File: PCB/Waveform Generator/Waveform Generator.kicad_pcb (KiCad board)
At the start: 4 copper layers, 124 parts, among them J1 Power input, J10 I2C1, J11 5001, J12 5001, J13 5001, J14 5001, J15 5001, J16 5001, J17 5001, J18 5001, J2 RS485, J3 USB_B_Micro, J4 Signal 1, J5 Signal 2, J6 SWD, J7 USART1, J8 TIMER, J9 ADC, Q0 AO3401A, Q1 Q_NPN_BCE, Q2 Q_NPN_BCE, Q3 Q_PNP_BCE, Q4 Q_NPN_BCE, Q5 Q_NPN_BCE, Q6 Q_NPN_BCE, SW1 SW_SPDT, SW2 RESET Button, SW3 SW_SPDT, SW4 Btn1, SW5 Btn1, SW6 Btn1, U1 STM32F405RGT6, U2 MAX485E, U3 USBLC6-2SC6, U4 OPAMP, U5 OPAMP, U6 OPAMP, U7 OPAMP, U8 LM335ADT

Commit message: Starting PCB layout
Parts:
- removed U6, U7: OPAMP, Package_SO:MSOP-8-1EP_3x3mm_P0.65mm_EP1.68x1.88mm
- J12: value 5001 -> Signal 2; footprint Extra Components:5001 Test Point -> TerminalBlock_MetzConnect:TerminalBlock_MetzConnect_Type086_RT03402HBLC_1x02_P3.81mm_Horizontal
- J4: value Signal 1 -> 5001; footprint TerminalBlock_MetzConnect:TerminalBlock_MetzConnect_Type086_RT03402HBLC_1x02_P3.81mm_Horizontal -> Extra Components:5001 Test Point
- U4, U5: value OPAMP -> LTC2051HVIMS8; footprint Package_SO:MSOP-8-1EP_3x3mm_P0.65mm_EP1.68x1.88mm -> Package_SO:MSOP-8-1EP_3x3mm_P0.65mm_EP1.73x1.85mm
- moved R13 307.6 mm to (479.3, -138.4)
- moved C13 289.1 mm to (511.3, -121.9)
- moved C12 273.3 mm to (511.8, -105.4)
- moved C11 272.4 mm to (504.2, -127.0)
- moved R12 233.5 mm to (416.6, -94.0)
- moved J15 210.3 mm to (195.4, -100.2)
- moved R23 209.4 mm to (332.4, -122.6)
- moved R27 209.4 mm to (338.2, -122.6)
- moved R25 209.4 mm to (335.3, -122.6)
- moved C25 200.5 mm to (408.5, -85.1)
- moved Q4 199.0 mm to (307.3, -161.3)
- moved R30 198.3 mm to (365.7, 112.4)
- moved R32 198.3 mm to (371.5, 112.4)
- moved R31 198.3 mm to (368.6, 112.4)
- moved R29 197.9 mm to (365.3, 106.7)
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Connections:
- J11 pad 1: (no net) -> Net-(J11-Pad1)
- J12 pad 1: (no net) -> Net-(J11-Pad1)
- J5 pad 1: Net-(J5-Pad1) -> Net-(J4-Pad1)
- R22 pad 1: Net-(J5-Pad1) -> Net-(J11-Pad1)
- U4 pad 1: GND -> Net-(R16-Pad1)
- U4 pad 3: Net-(R16-Pad1) -> GND
- U4 pad 4: +5V -> -5V
- U4 pad 5: -5V -> GND
- U4 pad 6: (no net) -> Net-(C28-Pad2)
- U4 pad 7: (no net) -> Net-(J4-Pad1)
- U4 pad 8: (no net) -> +5V
- U5 pad 1: GND -> Net-(R20-Pad1)
- U5 pad 2: Net-(C28-Pad2) -> Net-(C29-Pad2)
- U5 pad 3: Net-(J4-Pad1) -> GND
- U5 pad 4: +5V -> -5V
- U5 pad 5: -5V -> GND
- U5 pad 6: (no net) -> Net-(C30-Pad2)
- U5 pad 7: (no net) -> Net-(J11-Pad1)
- U5 pad 8: (no net) -> +5V

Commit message: update!
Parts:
- moved J18 497.3 mm to (105.5, 74.3)
- moved H2 466.8 mm to (107.0, 139.2)
- moved H3 460.5 mm to (107.6, 62.2)
- moved SW3 448.7 mm to (106.8, 98.9), turned to 270 degrees
- moved SW6 439.4 mm to (178.3, 141.0), turned to 90 degrees
- moved R13 437.3 mm to (112.5, 99.7)
- moved C11 425.0 mm to (168.9, 134.2), turned to 180 degrees
- moved SW5 421.7 mm to (187.4, 140.3), turned to 90 degrees
- moved C13 419.8 mm to (178.5, 134.0), turned to 180 degrees
- moved SW2 417.4 mm to (149.4, 115.5)
- moved SW4 410.0 mm to (168.8, 140.9), turned to 90 degrees
- moved C12 403.2 mm to (187.0, 133.5), turned to 180 degrees
- moved H4 377.5 mm to (218.9, 142.1)
- moved U8 376.8 mm to (148.8, 94.9)
- moved J17 376.7 mm to (156.8, 93.2)
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
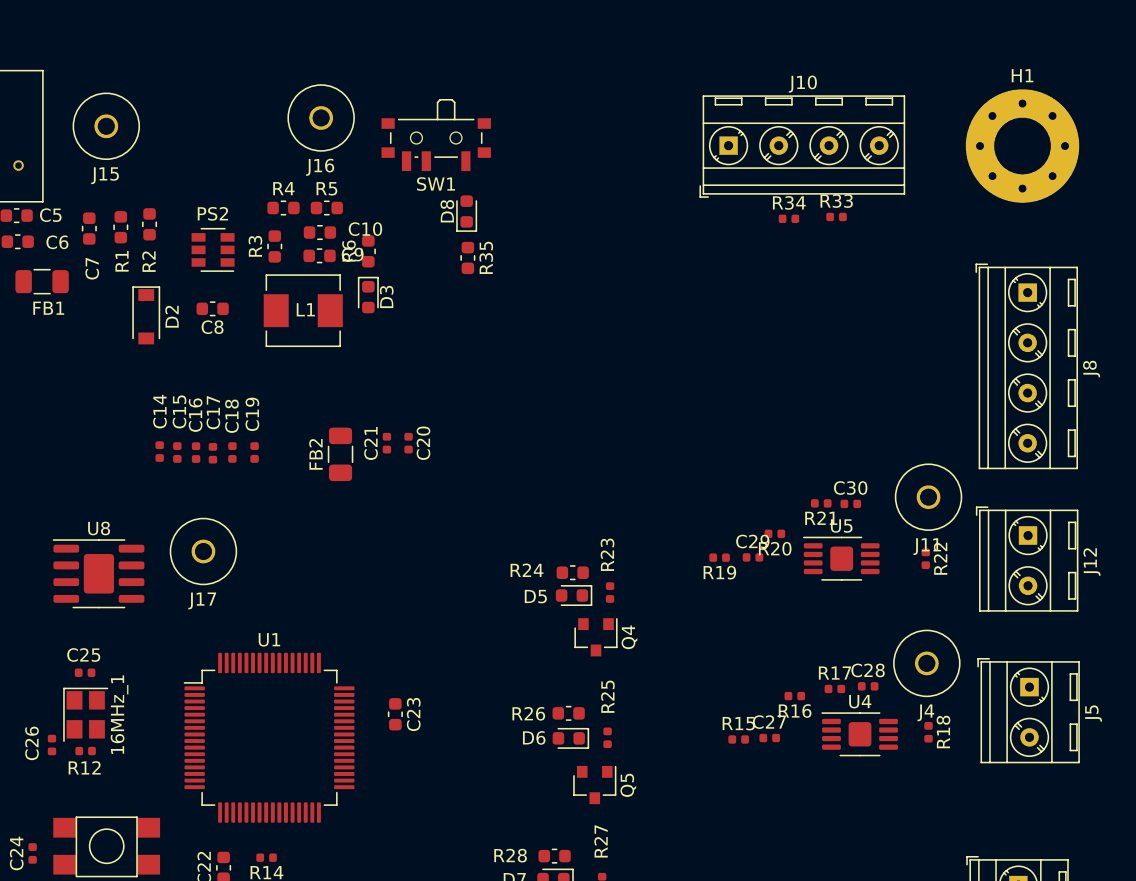
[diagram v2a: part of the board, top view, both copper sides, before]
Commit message: Updating op-amps and powersupply
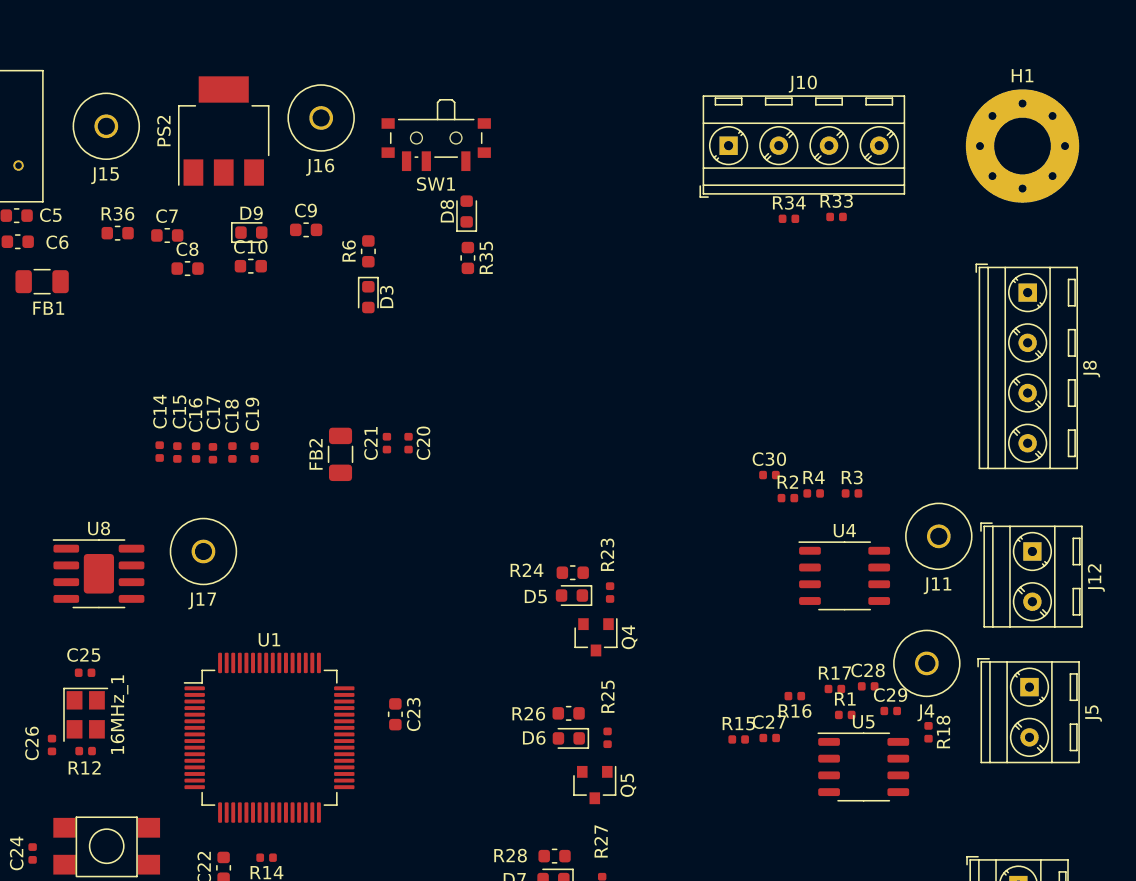
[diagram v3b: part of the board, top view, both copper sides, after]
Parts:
- removed D2: B5819W, Diode_SMD:D_SOD-123
- removed L1: 10u, Inductor_SMD:L_Sunlord_MWSA0518_5.4x5.2mm
- removed R19, R20, R21, R22: 1k, Resistor_SMD:R_0402_1005Metric
- removed R5: 270, Resistor_SMD:R_0603_1608Metric
- added D9: GREEN, LED_SMD:LED_0603_1608Metric, F.Cu at (160.4, 69.0)
- added R36: 1k, Resistor_SMD:R_0603_1608Metric, F.Cu at (150.2, 69.0)
- C8: value 10n -> 0.1u
- C9: value 10u -> 0.1u
- PS1: value ITP0312D05 -> ITP0324D05
- PS2: value MP2359DJ-LF-Z -> AMS1117-3.3; footprint Package_TO_SOT_SMD:SOT-23-6 -> Package_TO_SOT_SMD:SOT-223-3_TabPin2
- R1: value 100k -> 1k; footprint Resistor_SMD:R_0603_1608Metric -> Resistor_SMD:R_0402_1005Metric
- R2: value 68k -> 1k; footprint Resistor_SMD:R_0603_1608Metric -> Resistor_SMD:R_0402_1005Metric
- R3: value 47k -> 1k; footprint Resistor_SMD:R_0603_1608Metric -> Resistor_SMD:R_0402_1005Metric
- R4: value 15k -> 1k; footprint Resistor_SMD:R_0603_1608Metric -> Resistor_SMD:R_0402_1005Metric
- U4, U5: value LTC2051HVIMS8 -> OPA1602; footprint Package_SO:MSOP-8-1EP_3x3mm_P0.65mm_EP1.73x1.85mm -> Package_SO:SOP-8_3.9x4.9mm_P1.27mm
- moved R1 66.3 mm to (205.4, 105.6), turned to 0 degrees
- moved R2 52.7 mm to (201.1, 89.2), turned to 0 degrees
- moved R3 47.6 mm to (206.0, 88.8), turned to 0 degrees
- moved R4 45.7 mm to (203.1, 88.8)
- moved U5 15.9 mm to (206.8, 109.5)
- moved C29 15.7 mm to (208.9, 105.3)
- moved U4 12.1 mm to (205.4, 95.0)
- moved PS2 9.06 mm to (158.3, 61.3), turned to 90 degrees
- moved C30 6.55 mm to (199.7, 87.4)
- moved C7 5.94 mm to (154.0, 69.2), turned to 0 degrees
- moved C10 5.83 mm to (160.4, 71.6)
- moved C8 3.60 mm to (155.6, 71.7), turned to 0 degrees
- moved J11 3.07 mm to (212.6, 92.0)
- moved C9 2.22 mm to (164.6, 68.8)
- moved J12 1.25 mm to (219.7, 93.2)
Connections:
- C10 pad 1: GND -> Net-(C10-Pad1)
- C10 pad 2: Net-(C10-Pad2) -> GND
- C7 pad 1: GND -> +5V
- C7 pad 2: +5V -> GND
- C8 pad 1: Net-(C8-Pad1) -> +5V
- C8 pad 2: Net-(C8-Pad2) -> GND
- C9 pad 1: GND -> Net-(C10-Pad1)
- C9 pad 2: Net-(C10-Pad2) -> GND
- D3 pad 2: Net-(C10-Pad2) -> Net-(C10-Pad1)
- J16 pad 1: Net-(C10-Pad2) -> Net-(C10-Pad1)
- PS2 pad 1: Net-(C8-Pad1) -> (no net)
- PS2 pad 2: GND -> Net-(C10-Pad1)
- PS2 pad 3: Net-(PS2-Pad3) -> +5V
- R1 pad 1: +5V -> Net-(C29-Pad1)
- R1 pad 2: Net-(PS2-Pad4) -> Net-(R1-Pad2)
- R16 pad 1: Net-(R16-Pad1) -> Net-(C27-Pad2)
- R16 pad 2: Net-(C27-Pad2) -> Net-(R16-Pad2)
- R17 pad 2: Net-(R16-Pad1) -> Net-(R16-Pad2)
- R2 pad 1: Net-(PS2-Pad4) -> Net-(C30-Pad1)
- R2 pad 2: GND -> DAC_OUT2
- R3 pad 1: Net-(C10-Pad2) -> Net-(J11-Pad1)
- R3 pad 2: Net-(PS2-Pad3) -> Net-(C29-Pad2)
- R4 pad 1: Net-(PS2-Pad3) -> Net-(C30-Pad2)
- R4 pad 2: Net-(R4-Pad2) -> Net-(R1-Pad2)
- SW1 pad 2: Net-(C10-Pad2) -> Net-(C10-Pad1)
- U4 pad 1: Net-(R16-Pad1) -> Net-(R16-Pad2)
- U5 pad 1: Net-(R20-Pad1) -> Net-(R1-Pad2)
- U5 pad 2: Net-(C29-Pad2) -> Net-(C30-Pad2)
- U5 pad 6: Net-(C30-Pad2) -> Net-(C29-Pad2)

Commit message: Making updates to schematic
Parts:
- moved C29 15.0 mm to (208.2, 90.3)
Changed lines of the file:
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@@
   )
   (module Capacitor_SMD:C_0402_1005Metric (layer F.Cu)
-    (at 208.9 105.3)
+    (at 208.165 90.3)
     (descr "Capacitor SMD 0402 (1005 Metric), square (rectangular) end terminal, IPC_7351 nominal, (Body size source: http://www.tortai-tech.com/upload/download/2011102023233369053.pdf), generated with kicad-footprint-generator")
     (tags capacitor)
@@
       (effects (font (size 1 1) (thickness 0.15)))
     )
+    (fp_line (start -0.5 0.25) (end -0.5 -0.25) (layer F.Fab) (width 0.1))
+    (fp_line (start -0.5 -0.25) (end 0.5 -0.25) (layer F.Fab) (width 0.1))
+    (fp_line (start 0.5 -0.25) (end 0.5 0.25) (layer F.Fab) (width 0.1))
+    (fp_line (start 0.5 0.25) (end -0.5 0.25) (layer F.Fab) (width 0.1))
+    (fp_line (start -0.93 0.47) (end -0.93 -0.47) (layer F.CrtYd) (width 0.05))
+    (fp_line (start -0.93 -0.47) (end 0.93 -0.47) (layer F.CrtYd) (width 0.05))
+    (fp_line (start 0.93 -0.47) (end 0.93 0.47) (layer F.CrtYd) (width 0.05))
+    (fp_line (start 0.93 0.47) (end -0.93 0.47) (layer F.CrtYd) (width 0.05))
     (fp_text user %R (at 0 0) (layer F.Fab)
       (effects (font (size 0.25 0.25) (thickness 0.04)))
     )
-    (fp_line (start 0.93 0.47) (end -0.93 0.47) (layer F.CrtYd) (width 0.05))
-    (fp_line (start 0.93 -0.47) (end 0.93 0.47) (layer F.CrtYd) (width 0.05))
-    (fp_line (start -0.93 -0.47) (end 0.93 -0.47) (layer F.CrtYd) (width 0.05))
-    (fp_line (start -0.93 0.47) (end -0.93 -0.47) (layer F.CrtYd) (width 0.05))
-    (fp_line (start 0.5 0.25) (end -0.5 0.25) (layer F.Fab) (width 0.1))
-    (fp_line (start 0.5 -0.25) (end 0.5 0.25) (layer F.Fab) (width 0.1))
-    (fp_line (start -0.5 -0.25) (end 0.5 -0.25) (layer F.Fab) (width 0.1))
-    (fp_line (start -0.5 0.25) (end -0.5 -0.25) (layer F.Fab) (width 0.1))
+    (pad 1 smd roundrect (at -0.485 0) (size 0.59 0.64) (layers F.Cu F.Paste F.Mask) (roundrect_rratio 0.25)
+      (net 20 "Net-(C29-Pad1)"))
     (pad 2 smd roundrect (at 0.485 0) (size 0.59 0.64) (layers F.Cu F.Paste F.Mask) (roundrect_rratio 0.25)
       (net 86 "Net-(R1-Pad2)"))
-    (pad 1 smd roundrect (at -0.485 0) (size 0.59 0.64) (layers F.Cu F.Paste F.Mask) (roundrect_rratio 0.25)
-      (net 20 "Net-(C29-Pad1)"))
     (model ${KISYS3DMOD}/Resistor_SMD.3dshapes/R_0402_1005Metric.wrl
       (at (xyz 0 0 0))

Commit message: Making progress with PCB layout
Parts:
- added D10: RED, LED_SMD:LED_0603_1608Metric, F.Cu at (306.9, 133.3)
- added D2: GREEN, LED_SMD:LED_0603_1608Metric, F.Cu at (311.0, 133.3)
- added J19: ADC_2, Extra Components:5mm Pitch, 2 Way Terminal Block, F.Cu at (331.9, 98.2)
- added J20: TIMER_1, Extra Components:5mm Pitch, 2 Way Terminal Block, F.Cu at (313.4, 116.7)
- added J21: I2C1_1, Extra Components:5mm Pitch, 2 Way Terminal Block, F.Cu at (325.6, 114.3)
- added J22: TIMER_2, Extra Components:5mm Pitch, 2 Way Terminal Block, F.Cu at (344.0, 98.2)
- added J23: I2C1_2, Extra Components:5mm Pitch, 2 Way Terminal Block, F.Cu at (356.2, 98.2)
- added Q7: Q_NPN_BCE, Package_TO_SOT_SMD:SOT-23, F.Cu at (331.2, 127.2)
- added Q8: Q_NPN_BCE, Package_TO_SOT_SMD:SOT-23, F.Cu at (321.7, 131.9)
- added R19: 10k, Resistor_SMD:R_0402_1005Metric, F.Cu at (329.4, 130.6)
- added R20: 10k, Resistor_SMD:R_0402_1005Metric, F.Cu at (325.4, 133.1)
- added R21: 470, Resistor_SMD:R_0603_1608Metric, F.Cu at (325.9, 130.8)
- added R22: 470, Resistor_SMD:R_0603_1608Metric, F.Cu at (364.0, 94.0)
- added R37: 33, Resistor_SMD:R_0402_1005Metric, F.Cu at (338.9, 125.9)
- added R38: 33, Resistor_SMD:R_0402_1005Metric, F.Cu at (328.3, 133.1)
- added R39: 120, Resistor_SMD:R_0603_1608Metric, F.Cu at (335.4, 126.2)
- added R5: 10k, Resistor_SMD:R_0402_1005Metric, F.Cu at (111.5, 84.2)
- added SW7: SW_SPDT, Button_Switch_SMD:SW_SPDT_PCM12, F.Cu at (108.3, 84.1)
- added U10: USBLC6-2SC6, Package_TO_SOT_SMD:SOT-23-6, F.Cu at (317.0, 131.9)
- added U11: USBLC6-2SC6, Package_TO_SOT_SMD:SOT-23-6, F.Cu at (307.3, 129.6)
- added U6: USBLC6-2SC6, Package_TO_SOT_SMD:SOT-23-6, F.Cu at (321.7, 127.3)
- added U7: USBLC6-2SC6, Package_TO_SOT_SMD:SOT-23-6, F.Cu at (312.2, 129.6)
- added U9: USBLC6-2SC6, Package_TO_SOT_SMD:SOT-23-6, F.Cu at (326.6, 127.3)
- C22, C23: footprint Capacitor_SMD:C_0603_1608Metric -> Capacitor_SMD:C_0402_1005Metric
- C25, C26: value 12p -> 20p
- F1: value 250mA -> 300mA
- FB2: value 600 @ 600 MHz -> 600 @ 600MHz
- J10: value I2C1 -> USART1_2; footprint TerminalBlock_MetzConnect:TerminalBlock_MetzConnect_Type086_RT03404HBLC_1x04_P3.81mm_Horizontal -> Extra Components:5mm Pitch, 2 Way Terminal Block
- J2: value RS485 -> RS485_1; footprint TerminalBlock_MetzConnect:TerminalBlock_MetzConnect_Type086_RT03404HBLC_1x04_P3.81mm_Horizontal -> Extra Components:5mm Pitch, 2 Way Terminal Block
- J5: footprint TerminalBlock_MetzConnect:TerminalBlock_MetzConnect_Type086_RT03402HBLC_1x02_P3.81mm_Horizontal -> Extra Components:5mm Pitch, 2 Way Terminal Block
- J7: value USART1 -> RS485_2; footprint TerminalBlock_MetzConnect:TerminalBlock_MetzConnect_Type086_RT03404HBLC_1x04_P3.81mm_Horizontal -> Extra Components:5mm Pitch, 2 Way Terminal Block
- J8: value TIMER -> USART1_1; footprint TerminalBlock_MetzConnect:TerminalBlock_MetzConnect_Type086_RT03404HBLC_1x04_P3.81mm_Horizontal -> Extra Components:5mm Pitch, 2 Way Terminal Block
- J9: value ADC -> ADC_1; footprint TerminalBlock_MetzConnect:TerminalBlock_MetzConnect_Type086_RT03404HBLC_1x04_P3.81mm_Horizontal -> Extra Components:5mm Pitch, 2 Way Terminal Block
- U1: value STM32F405RGT6 -> STM32F427VITx; footprint Package_QFP:LQFP-64_10x10mm_P0.5mm -> Package_QFP:LQFP-100_14x14mm_P0.5mm
- U2: value MAX485E -> MAX485EESAT
- X1: renamed from 16MHz_1; value Y200 -> 25MHZ
- moved J2 217.5 mm to (361.9, 114.3), turned to 0 degrees
- moved C22 210.5 mm to (367.5, 93.7), turned to 0 degrees
- moved R14 202.9 mm to (363.5, 96.2), turned to 0 degrees
- moved C23 146.5 mm to (316.1, 128.3), turned to 0 degrees
- moved J7 142.0 mm to (349.8, 114.3), turned to 0 degrees
- moved J10 128.3 mm to (319.8, 98.2)
- moved J8 125.2 mm to (337.7, 114.3), turned to 0 degrees
- moved U1 121.2 mm to (281.4, 87.7)
- moved J9 82.7 mm to (301.3, 116.7), turned to 0 degrees
- moved J18 33.7 mm to (124.0, 46.2)
- moved D9 30.0 mm to (130.5, 71.2), turned to 90 degrees
- moved U3 23.8 mm to (113.7, 73.0), turned to 180 degrees
- moved J3 23.4 mm to (108.3, 73.1)
- moved R36 21.7 mm to (128.7, 71.2), turned to 90 degrees
- moved D3 19.1 mm to (152.4, 65.0), turned to 180 degrees
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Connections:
- C13 pad 2: BT3N_Input -> BTN3_Input
- J10 pad 1: +3V3 -> Net-(J10-Pad1)
- J10 pad 2: I2C1_SDA -> GND
- J12 pad 1: Net-(J11-Pad1) -> Net-(J12-Pad1)
- J3 pad 2: USB_CONN_D- -> Net-(J3-Pad2)
- J3 pad 3: USB_CONN_D+ -> Net-(J3-Pad3)
- J5 pad 1: Net-(J4-Pad1) -> Net-(J5-Pad1)
- J6 pad 3: GND -> Net-(J6-Pad3)
- J6 pad 5: GND -> Net-(J6-Pad5)
- J6 pad 9: GND -> Net-(J6-Pad9)
- J7 pad 1: +3V3 -> Net-(J14-Pad1)
- J7 pad 2: USART1_TX -> GND
- J8 pad 2: TIM1_CH1 -> Net-(J8-Pad2)
- J9 pad 2: ADC2_IN0 -> Net-(J9-Pad2)
- R14 pad 1: BOOT1 -> Net-(J6-Pad3)
- R33 pad 1: I2C1_SCL -> Net-(J23-Pad1)
- R34 pad 1: I2C1_SDA -> Net-(J21-Pad2)
- SW6 pad 1: BT3N_Input -> BTN3_Input
- U1 pad 1: +3V3 -> (no net)
- U1 pad 10: TEMP_SENSE -> GND
- U1 pad 11: (no net) -> +3V3
- U1 pad 12: GND -> HSE_IN
- U1 pad 13: +3.3VA -> HSE_OUT
- U1 pad 14: ADC2_IN0 -> NRST
- U1 pad 15: ADC1_IN1 -> MAX485_PWR
- U1 pad 16: USART2_TX -> MAX485_DE
- U1 pad 17: USART2_RX -> TEMP_SENSE
- U1 pad 18: GND -> (no net)
- U1 pad 20: DAC_OUT1 -> GND
- U1 pad 21: DAC_OUT2 -> +3.3VA
- U1 pad 22: TIM3_CH1 -> +3.3VA
- U1 pad 23: (no net) -> ADC2_IN0
- U1 pad 24: (no net) -> ADC1_IN1
- U1 pad 25: (no net) -> USART2_TX
- U1 pad 26: (no net) -> USART2_RX
- U1 pad 27: (no net) -> GND
- U1 pad 28: BOOT1 -> +3V3
- U1 pad 29: (no net) -> DAC_OUT1
- U1 pad 30: (no net) -> DAC_OUT2
- U1 pad 31: Net-(C22-Pad1) -> TIM3_CH1
- U1 pad 32: +3V3 -> (no net)
- U1 pad 34: LED3 -> (no net)
- U1 pad 35: LED2 -> (no net)
- U1 pad 36: LED1 -> (no net)
- U1 pad 37: BTN1_Input -> BOOT1
- U1 pad 38: BTN2_Input -> (no net)
- U1 pad 40: (no net) -> TIM1_CH1
- U1 pad 41: TIM1_CH1 -> (no net)
- U1 pad 42: USART1_TX -> (no net)
- U1 pad 43: USB_ID -> (no net)
- U1 pad 44: USB_D- -> (no net)
- U1 pad 45: USB_D+ -> (no net)
- U1 pad 46: SWDIO -> (no net)
- U1 pad 47: Net-(C23-Pad1) -> (no net)
- U1 pad 48: +3V3 -> (no net)
- U1 pad 49: SWCLK -> Net-(C22-Pad1)
- U1 pad 5: HSE_IN -> (no net)
- U1 pad 50: (no net) -> +3V3
- U1 pad 55: SW0 -> (no net)
- U1 pad 58: I2C1_SCL -> LED1
- U1 pad 59: USART1_RX -> LED2
- U1 pad 6: HSE_OUT -> +3V3
- U1 pad 60: BOOT0 -> LED3
- U1 pad 61: (no net) -> LED4
- U1 pad 62: I2C1_SDA -> LED5
- U1 pad 63: GND -> BTN3_Input
- U1 pad 64: +3V3 -> BTN2_Input
- U1 pad 7: NRST -> (no net)
- U1 pad 8: MAX485_PWR -> (no net)
- U1 pad 9: MAX485_DE -> (no net)
- U3 pad 1: USB_CONN_D- -> USB_D+
- U3 pad 3: USB_CONN_D+ -> USB_D-
- U3 pad 4: USB_D+ -> Net-(J3-Pad2)
- U3 pad 5: +5V -> VBUS
- U3 pad 6: USB_D- -> Net-(J3-Pad3)

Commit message: Working on PCB layout
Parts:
- J10, J19, J21, J23, J8, J9: moved to B.Cu
- J12: footprint TerminalBlock_MetzConnect:TerminalBlock_MetzConnect_Type086_RT03402HBLC_1x02_P3.81mm_Horizontal -> Extra Components:5mm Pitch, 2 Way Terminal Block
- J5: value Signal 2 -> Signal 1
- moved J19 269.1 mm to (63.1, 84.9), turned to 90 degrees
- moved U7 243.9 mm to (71.5, 90.2), turned to 180 degrees
- moved J9 239.0 mm to (63.2, 96.2), turned to 90 degrees
- moved U9 204.4 mm to (122.5, 139.7), turned to 270 degrees
- moved U11 197.5 mm to (115.3, 83.3), turned to 90 degrees
- moved U6 195.8 mm to (130.6, 84.5), turned to 180 degrees
- moved J23 178.9 mm to (181.7, 58.7), turned to 270 degrees
- moved H2 170.3 mm to (-62.1, 119.1)
- moved H1 168.1 mm to (60.0, 7.40)
- moved U1 163.1 mm to (118.4, 95.8)
- moved J8 162.1 mm to (181.6, 70.8), turned to 270 degrees
- moved J21 158.6 mm to (181.8, 47.3), turned to 270 degrees
- moved J10 138.9 mm to (181.8, 82.5), turned to 270 degrees
- moved D8 137.9 mm to (51.0, 10.7), turned to 180 degrees
- moved R35 136.9 mm to (53.5, 11.4)
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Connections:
- U7 pad 1: ADC2_IN0 -> ADC1_IN1
- U7 pad 3: ADC1_IN1 -> ADC2_IN0
- U9 pad 1: Net-(J4-Pad1) -> Net-(J11-Pad1)
- U9 pad 3: Net-(J11-Pad1) -> Net-(J4-Pad1)

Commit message: PCB
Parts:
- added D11: BLUE, LED_SMD:LED_0603_1608Metric, F.Cu at (84.6, 128.1)
- J10, J19, J21, J23, J8, J9: moved to F.Cu
- R10: value 1k -> 470
- moved J2 296.2 mm to (66.4, 135.5), turned to 270 degrees
- moved J7 283.5 mm to (66.5, 124.0), turned to 270 degrees
- moved D4 132.9 mm to (76.2, 133.9), turned to 270 degrees
- moved R8 132.1 mm to (83.3, 137.7)
- moved U2 130.4 mm to (75.3, 129.5), turned to 180 degrees
- moved Q3 130.2 mm to (80.6, 137.4)
- moved R9 129.6 mm to (77.8, 135.6), turned to 90 degrees
- moved R7 128.9 mm to (86.8, 135.2), turned to 180 degrees
- moved Q2 128.9 mm to (86.0, 137.6)
- moved J14 128.8 mm to (74.3, 121.5), turned to 270 degrees
- moved Q1 121.2 mm to (82.0, 129.2), turned to 180 degrees
- moved R11 118.4 mm to (84.3, 130.8), turned to 270 degrees
- moved J13 115.5 mm to (74.3, 138.1), turned to 270 degrees
- moved R10 114.9 mm to (86.2, 128.1), turned to 270 degrees
- moved U6 33.9 mm to (164.4, 81.9), turned to 0 degrees
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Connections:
- R10 pad 2: DE -> Net-(D11-Pad2)

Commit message: Updating PCB layout
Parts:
- moved R39 321.8 mm to (14.5, 102.5), turned to 90 degrees
- moved R14 317.5 mm to (48.9, 53.6), turned to 180 degrees
- moved C22 316.2 mm to (51.4, 86.2)
- moved J20 291.6 mm to (76.8, 99.9), turned to 90 degrees
- moved R19 288.7 mm to (51.1, 53.6)
- moved R20 281.3 mm to (54.9, 56.0), turned to 270 degrees
- moved J22 278.8 mm to (76.8, 111.2), turned to 90 degrees
- moved C23 265.9 mm to (56.5, 70.9), turned to 270 degrees
- moved U10 252.8 mm to (67.8, 89.4)
- moved R22 232.5 mm to (135.4, 51.5), turned to 180 degrees
- moved SW6 224.5 mm to (19.5, 121.5), turned to 270 degrees
- moved SW5 223.3 mm to (29.6, 121.3), turned to 270 degrees
- moved C13 220.5 mm to (19.3, 126.5), turned to 0 degrees
- moved C12 218.5 mm to (29.6, 126.5), turned to 0 degrees
- moved R37 216.6 mm to (137.9, 45.1)
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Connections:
- U1 pad 90: SWDIO -> (no net)
